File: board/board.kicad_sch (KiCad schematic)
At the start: 4 parts, among them J1 002_SPI, J2 007_ADC, J3 007_ADC

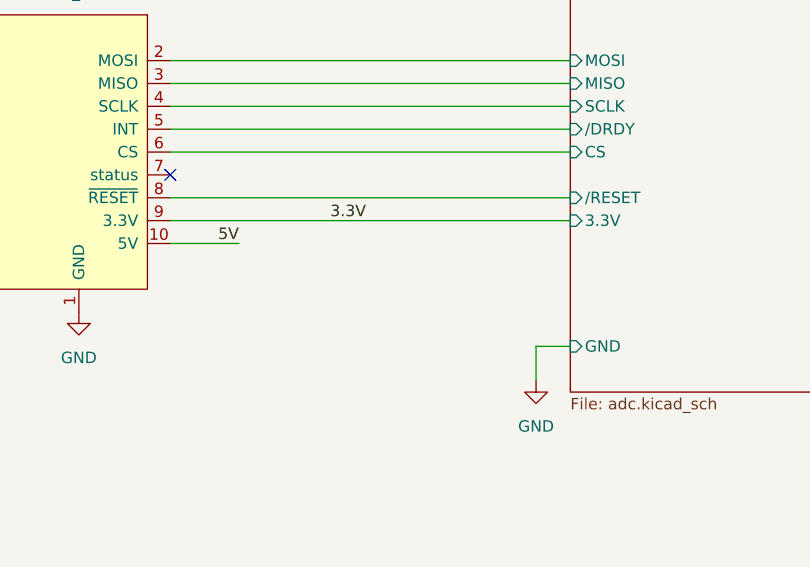
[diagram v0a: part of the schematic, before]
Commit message: added ground pours, a picture and decoupling for the oscillator
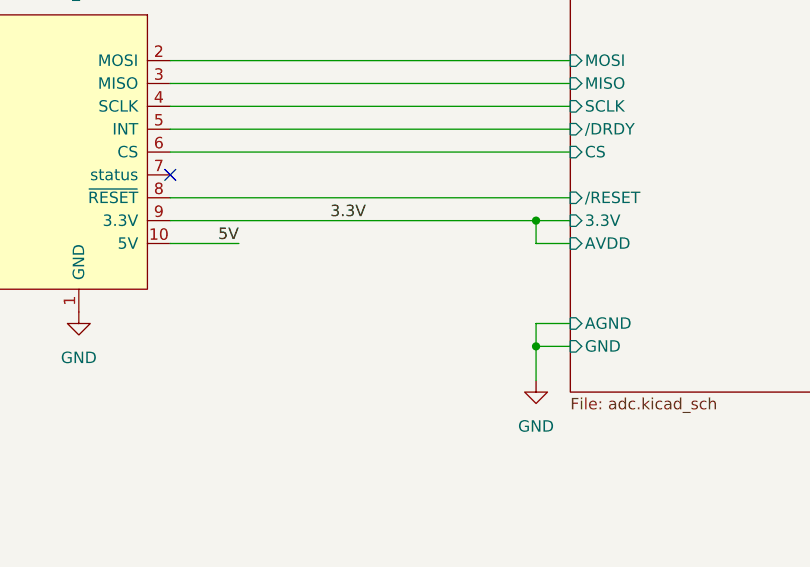
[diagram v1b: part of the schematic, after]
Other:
- sheet adc ports: added AGND, AVDD; removed none
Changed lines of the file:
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@@
 (kicad_sch (version 20211123) (generator eeschema)
   (paper "A4")
+  (junction (at 110.49 115.57) (diameter 0) (color 0 0 0 0)
+  )
+  (junction (at 110.49 129.54) (diameter 0) (color 0 0 0 0)
+  )
   (no_connect (at 217.17 81.28))
   (no_connect (at 69.85 110.49))
@@
     (stroke (width 0) (type default) (color 0 0 0 0))
   )
-  (wire (pts (xy 69.85 115.57) (xy 114.3 115.57))
+  (wire (pts (xy 114.3 118.11) (xy 110.49 118.11))
+    (stroke (width 0) (type default) (color 0 0 0 0))
+  )
+  (wire (pts (xy 69.85 115.57) (xy 110.49 115.57))
+    (stroke (width 0) (type default) (color 0 0 0 0))
+  )
+  (wire (pts (xy 110.49 115.57) (xy 114.3 115.57))
     (stroke (width 0) (type default) (color 0 0 0 0))
   )
@@
   )
   (wire (pts (xy 69.85 100.33) (xy 114.3 100.33))
+    (stroke (width 0) (type default) (color 0 0 0 0))
+  )
+  (wire (pts (xy 114.3 127) (xy 110.49 127))
+    (stroke (width 0) (type default) (color 0 0 0 0))
+  )
+  (wire (pts (xy 110.49 118.11) (xy 110.49 115.57))
+    (stroke (width 0) (type default) (color 0 0 0 0))
+  )
+  (wire (pts (xy 110.49 127) (xy 110.49 129.54))
     (stroke (width 0) (type default) (color 0 0 0 0))
   )
@@
       (effects (font (size 1.27 1.27)) (justify right))
     )
+    (pin "AVDD" input (at 114.3 118.11 180)
+      (effects (font (size 1.27 1.27)) (justify left))
+    )
+    (pin "AGND" input (at 114.3 127 180)
+      (effects (font (size 1.27 1.27)) (justify left))
+    )
   )
   (sheet_instances
@@
       (reference "C4") (unit 1) (value "100nF") (footprint "Capacitor_SMD:C_0603_1608Metric")
     )
+    (path "/767ce4c6-0e55-4543-92f0-34cb8237a544/8ff5d142-baab-4c59-8625-8f4a54fec020"
+      (reference "C5") (unit 1) (value "100nF") (footprint "Capacitor_SMD:C_0603_1608Metric")
+    )
     (path "/58e37701-2d7e-416e-8006-dcb5291155a8"
